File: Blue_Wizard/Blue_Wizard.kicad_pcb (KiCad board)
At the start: 2 copper layers, 108 x 95.2 mm, 47 parts, among them J1 Conn_ARM_JTAG_SWD_10, J10 Left Keywell Header, J11 Conn_01x02, J12 10137062-00021LF, J13 Conn_01x01, J14 Conn_01x02, J2 Conn_01x05, J3 Right FN, J4 Right Keywell, J5 Right Thumb Cluster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

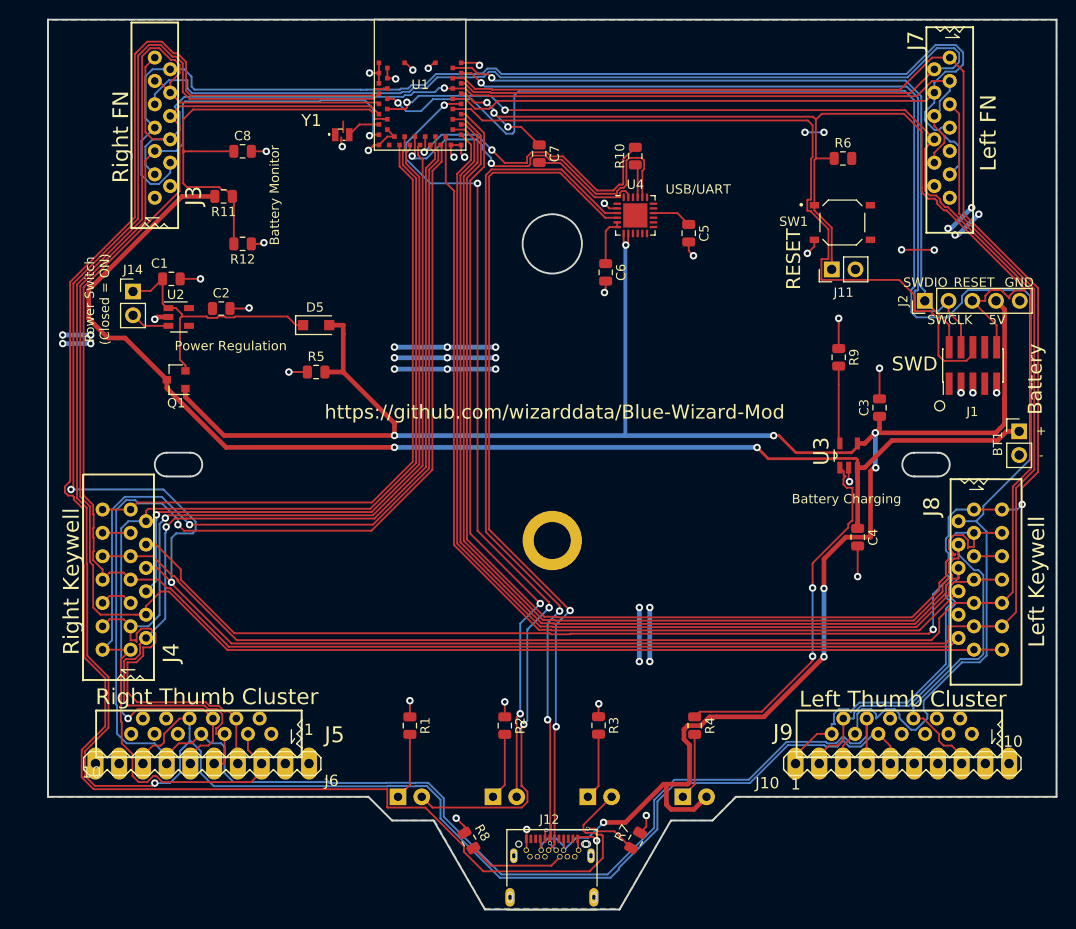
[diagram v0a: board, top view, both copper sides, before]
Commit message: convert files for new versions of KiCad
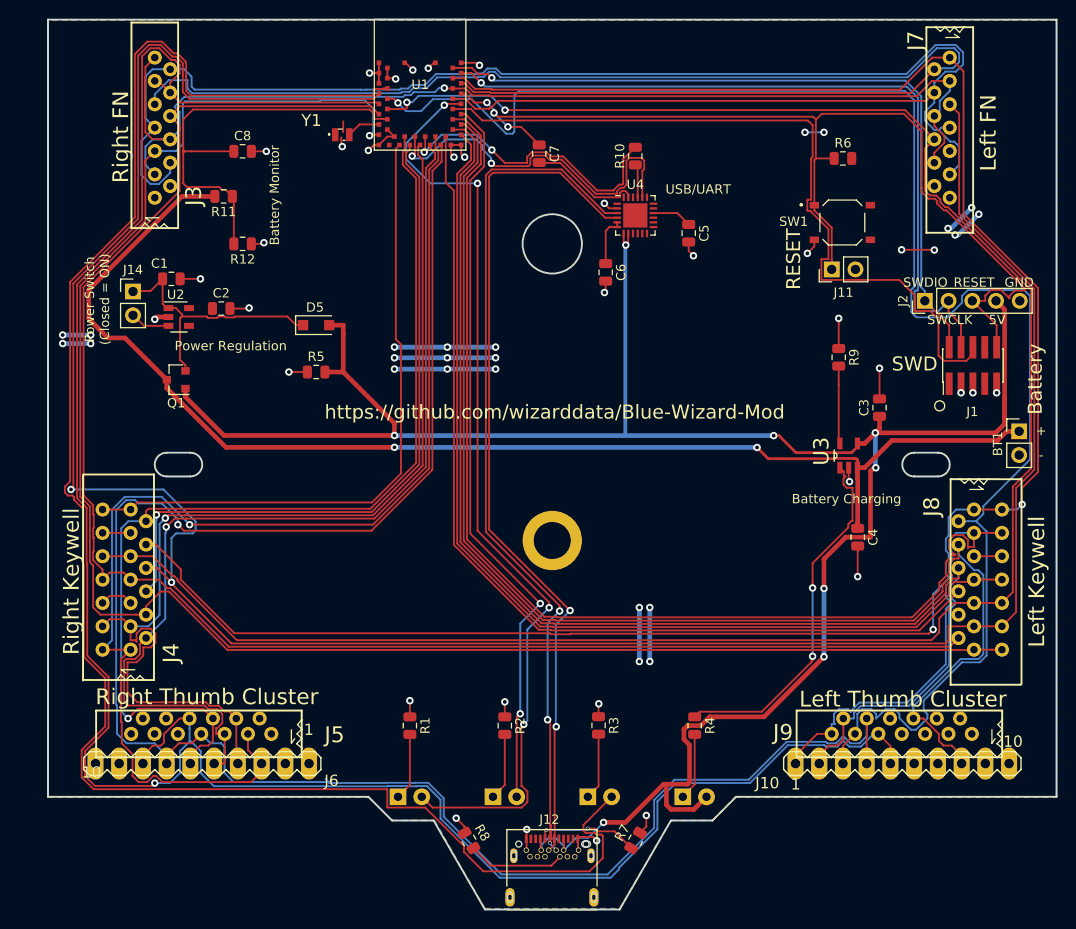
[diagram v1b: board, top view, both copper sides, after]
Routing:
- net C2: track 69.8 -> 69.1 mm
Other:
- net class Default removed
- net class Power removed
- net class USB5V removed
